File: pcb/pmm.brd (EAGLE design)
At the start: 30 x 30 mm, 25 parts, among them IC3 STM32F042F4, SW3 324_SW, SW4 324_SW, U2 USBC_16P, U4 XC6206_DEV

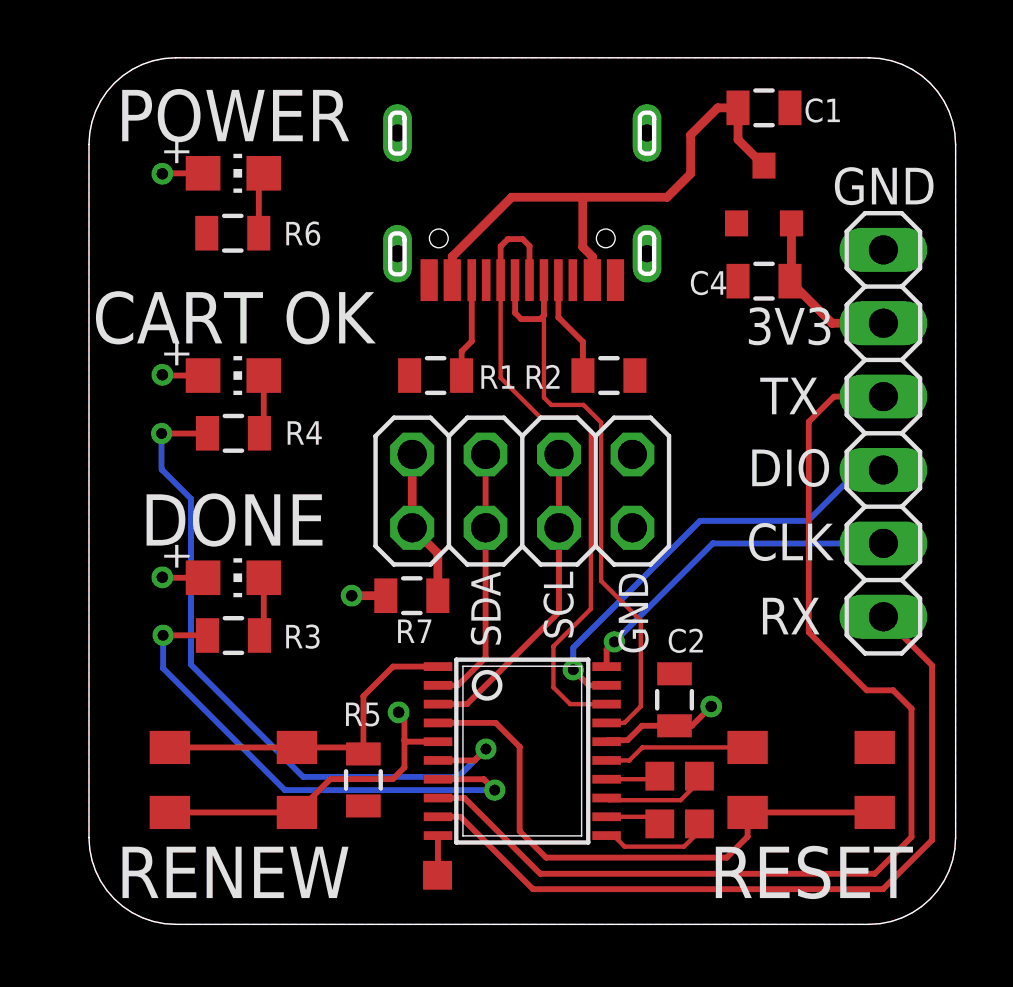
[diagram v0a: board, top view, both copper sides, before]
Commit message: fixed card edge connector footprint
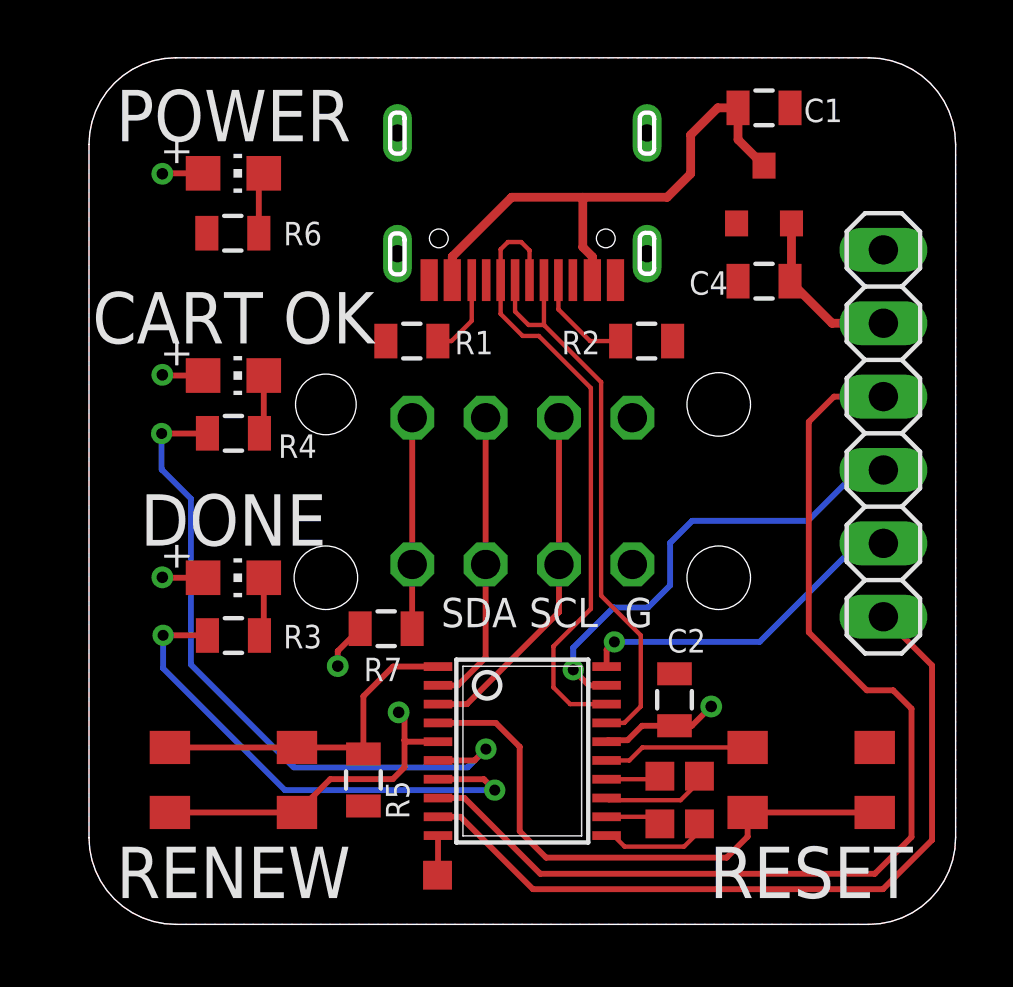
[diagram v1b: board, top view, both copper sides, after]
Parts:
- JP1: device pinhead:2X04 -> pmm:PINHEAD_2X04
- moved R2 1.77 mm to (19.3, 20.2)
- moved R1 1.45 mm to (11.2, 20.2)
- moved R7 1.45 mm to (10.3, 10.2)
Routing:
- net N$10: track 5.26 -> 7.31 mm
- net SCL: track 11.0 -> 12.2 mm
- net N$2: track 9.08 -> 10.4 mm
- net N$4: track 15.4 -> 16.3 mm
- net USB_DN: track 20.5 -> 19.8 mm
- net USB_DP: track 22.3 -> 21.7 mm
- net N$31: track 3.45 -> 2.87 mm
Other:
- board text added: "Bob Dishwasher Cassette Rewinder"
- board text added: "G"
- board text removed: "Bob Dishwasher Cassette Renewer"
